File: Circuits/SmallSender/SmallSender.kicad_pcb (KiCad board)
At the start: 2 copper layers, 28 x 57.5 mm, 12 parts, among them CN1 WRITER, SW1 SW_PUSH, SW2 REED SW, U1 LITE_LITE, U2 HN2S01FU

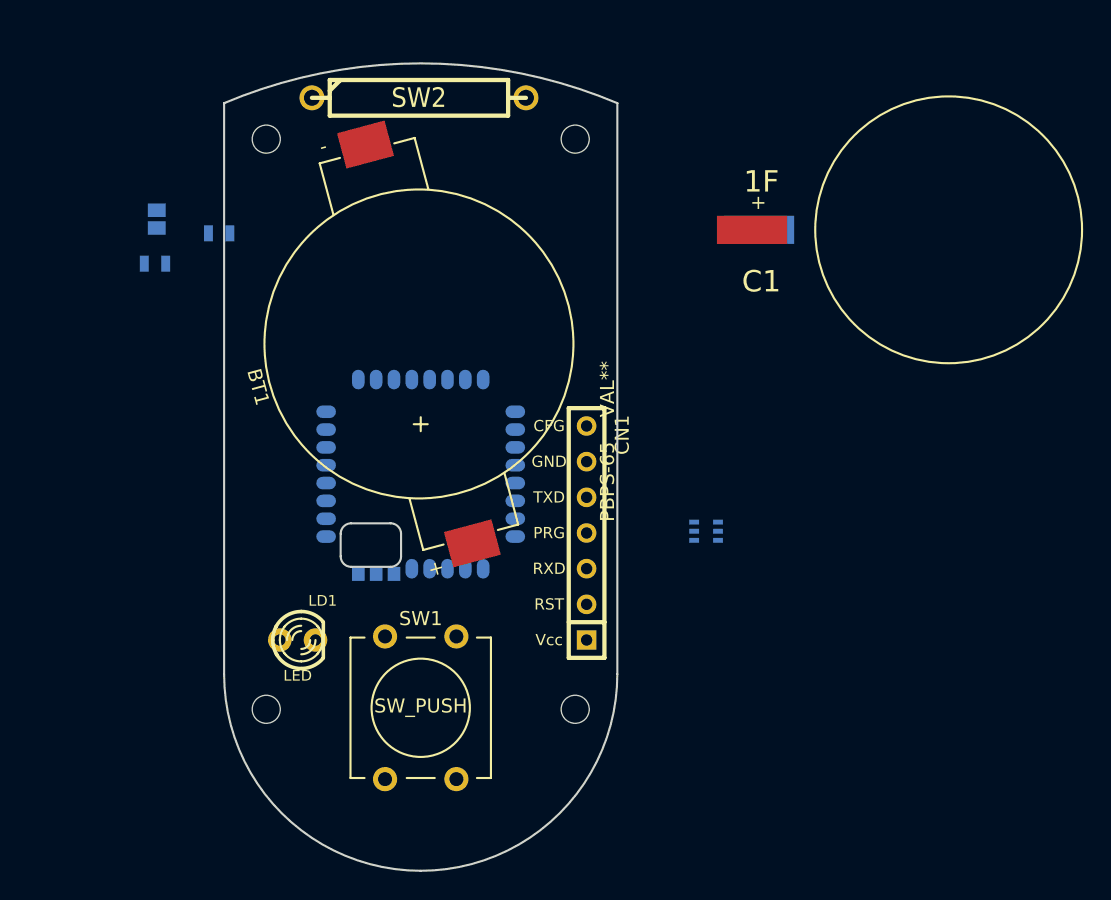
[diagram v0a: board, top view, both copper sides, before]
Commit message: Replaced EDLC.
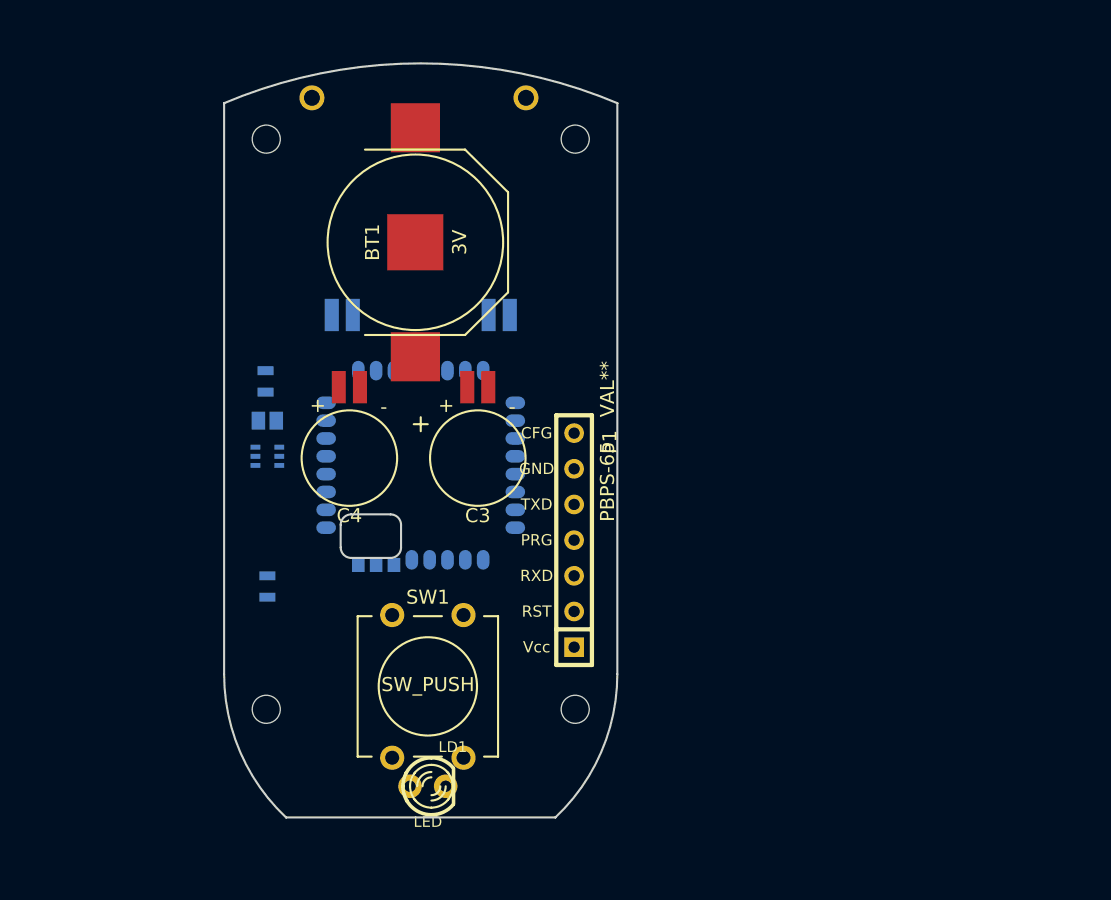
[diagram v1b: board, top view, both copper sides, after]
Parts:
- removed CN1: WRITER, 2211R-07G-LP
- added C2: 0.22, DCK-3R3E224-E, B.Cu at (34.5, 29.0)
- added C3: 0.22, DCK-3R3E224-E, F.Cu at (44.2, 44.2)
- added C4: 0.22, DCK-3R3E224-E, F.Cu at (35.1, 44.2)
- added P1: WRITER-VCC, WRITE-7P, F.Cu at (51.1, 50.0)
- BT1: footprint SMTU2032 -> BK-885
- C1: value 1F -> 0.22; footprint SE-5R5-D105VYV -> DCK-3R3E224-E; moved to B.Cu
- SW2: moved to B.Cu
- U1: value LITE_LITE -> TWE_LITE_SMD
- moved C1 32.0 mm to (45.7, 29.0)
- moved U2 31.7 mm to (29.2, 44.1), turned to 180 degrees
- moved R2 25.4 mm to (29.2, 53.3), turned to 270 degrees
- moved JP1 16.4 mm to (29.2, 41.5), turned to 90 degrees
- moved LD1 13.9 mm to (40.6, 67.6)
- moved R1 11.5 mm to (29.1, 38.7), turned to 270 degrees
- moved BT1 7.24 mm to (39.8, 28.8), turned to 90 degrees
- moved SW1 1.61 mm to (40.6, 60.5)
- moved U1 0.63 mm to (40.1, 44.7)
- turned SW2 to 180 degrees
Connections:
- R2 pad 1: /LED -> /Vcc
- R2 pad 2: /Vcc -> /LED
- U1 pad 12: /M1 -> /CFG
- U1 pad 28: (no net) -> GND
- U1 pad 30: (no net) -> GND
- U1 pad 31: (no net) -> GND
- U1 pad 32: (no net) -> GND
- U1 pad 8: /RX -> /TXD
- U1 pad 9: /TX -> /RXD
- U2 pad 6: /DC3V -> /Vcc
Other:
- board size 28 x 57.5 mm -> 28 x 53.7 mm

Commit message: Added a 3D model of PS-65.
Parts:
- BT1: value 3V -> CR1220

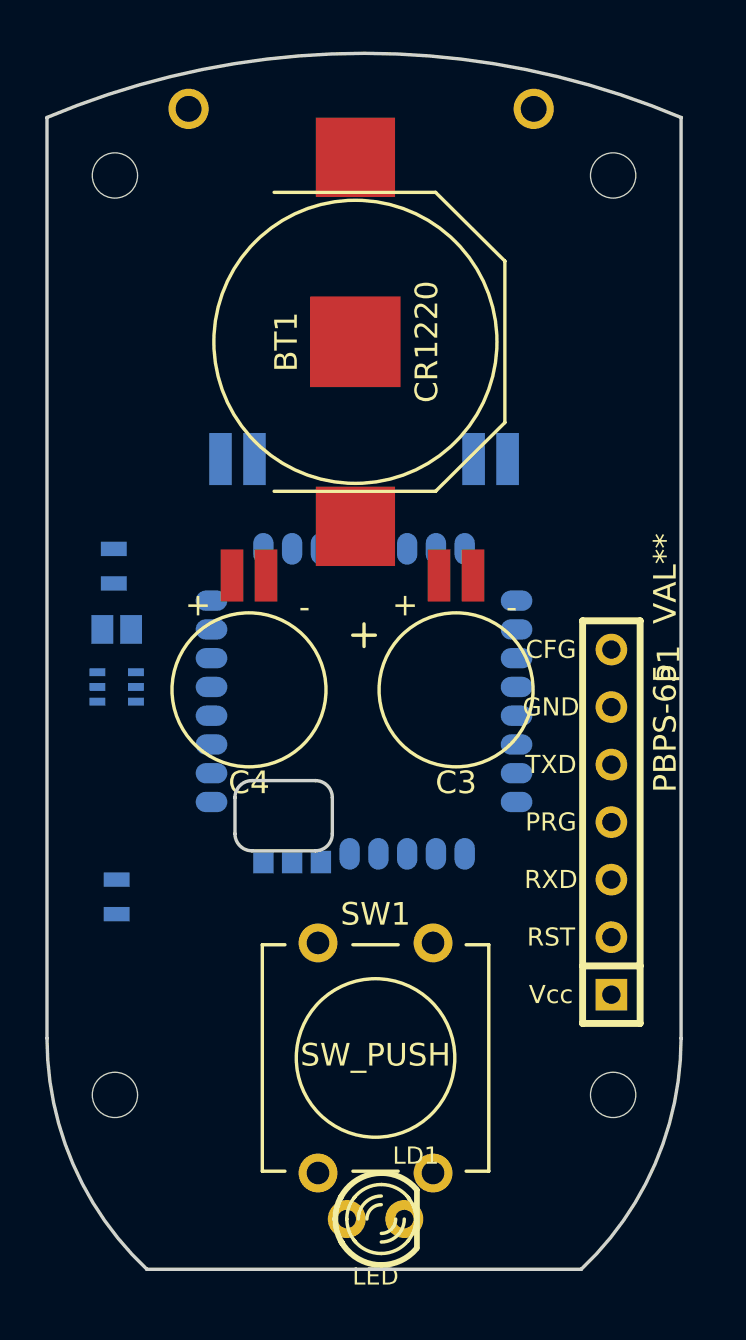
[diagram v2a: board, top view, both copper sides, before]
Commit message: Changed battery holder. Added more EDLC.
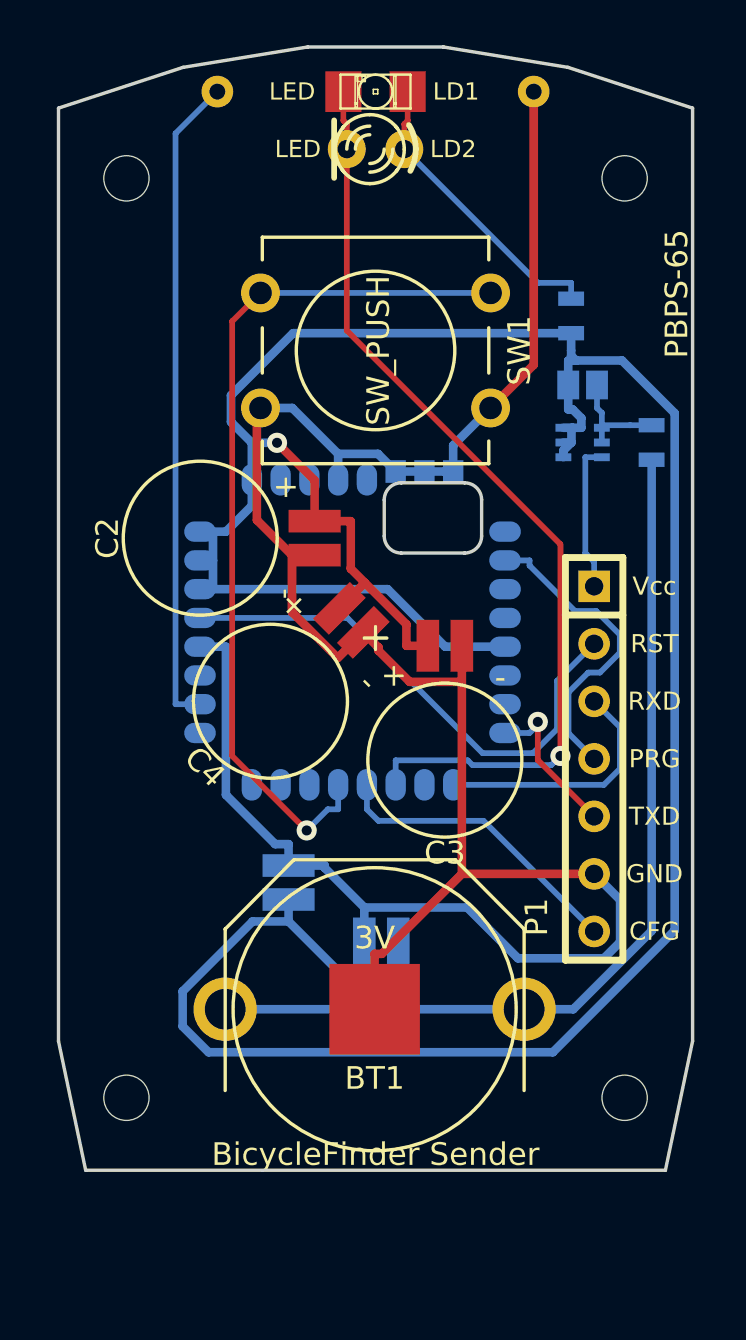
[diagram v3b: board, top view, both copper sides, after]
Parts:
- added C5: 0.22, DCK-3R3E224-E, B.Cu at (31.8, 52.7)
- added LD1: LED, LED-1206, F.Cu at (40.6, 17.8)
- BT1: value CR1220 -> 3V; footprint BK-885 -> BK-890
- C2: moved to F.Cu
- PBPS-65: value VAL** -> BicycleFinder Sender
- SW2: footprint R6 -> REEDSW
- moved LD2 47.2 mm to (40.6, 20.3), turned to 180 degrees
- moved R2 32.6 mm to (49.3, 27.7), turned to 90 degrees
- moved C1 31.9 mm to (40.9, 60.5), turned to 0 degrees
- moved SW1 31.2 mm to (40.6, 29.2), turned to 90 degrees
- moved BT1 29.5 mm to (40.6, 58.3), turned to 180 degrees
- moved R1 24.4 mm to (52.8, 33.3), turned to 90 degrees
- moved JP1 23.2 mm to (49.8, 30.7), turned to 270 degrees
- moved U2 23.2 mm to (49.8, 33.3), turned to 0 degrees
- moved C2 8.70 mm to (32.9, 37.5), turned to 90 degrees
- moved C3 3.14 mm to (43.7, 47.3)
- moved U1 3.09 mm to (39.6, 41.7), turned to 180 degrees
- moved P1 2.90 mm to (50.3, 47.2), turned to 270 degrees
- moved C4 1.07 mm to (36.0, 44.7), turned to 135 degrees
- moved SW2 0.99 mm to (40.6, 17.8), turned to 0 degrees
- moved PBPS-65 0.52 mm to (40.6, 41.9)
- renumbered LD1 to LD2
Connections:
- C4 pad 1: (no net) -> /Vcc
- P1 pad 1: /Vcc -> /3V3
- U1 pad 22: (no net) -> /Vcc
- U1 pad 23: (no net) -> /Vcc
- U1 pad 24: (no net) -> /Vcc
- U1 pad 25: (no net) -> /Vcc
- U2 pad 6: /Vcc -> /3V3
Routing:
- net /Vcc: track 0.00 -> 133.9 mm, vias 0 -> 1
- net GND: track 0.00 -> 107.3 mm
- net /DO4: track 0.00 -> 41.9 mm, vias 0 -> 1
- net /3V: track 0.00 -> 41.1 mm
- net /DI1: track 0.00 -> 38.6 mm, vias 0 -> 1
- net /DI4: track 0.00 -> 28.9 mm
- net /RST: track 0.00 -> 23.1 mm
- net /PRG: track 0.00 -> 13.8 mm
- net /CFG: track 0.00 -> 13.3 mm
- net /LED: track 0.00 -> 13.1 mm
- net /RXD: track 0.00 -> 11.1 mm
- net /TXD: track 0.00 -> 6.92 mm, vias 0 -> 1
- net /3V3: track 0.00 -> 6.59 mm
- net /CHG: track 0.00 -> 4.83 mm
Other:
- board size 28 x 53.7 mm -> 28 x 49.6 mm
- net class Power added: clearance 0.254, trace_width 0.381, via_dia 0.889, via_drill 0.635

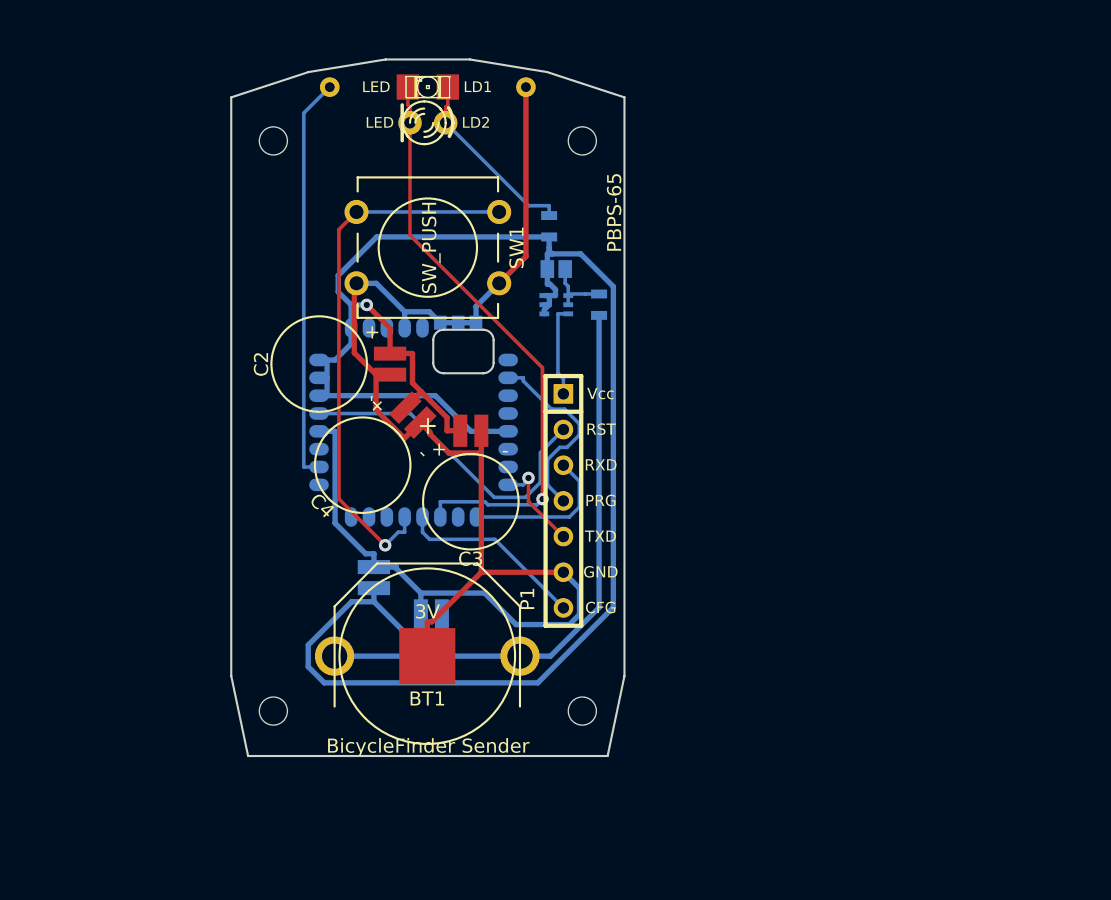
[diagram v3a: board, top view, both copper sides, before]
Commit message: Changed EDLC.
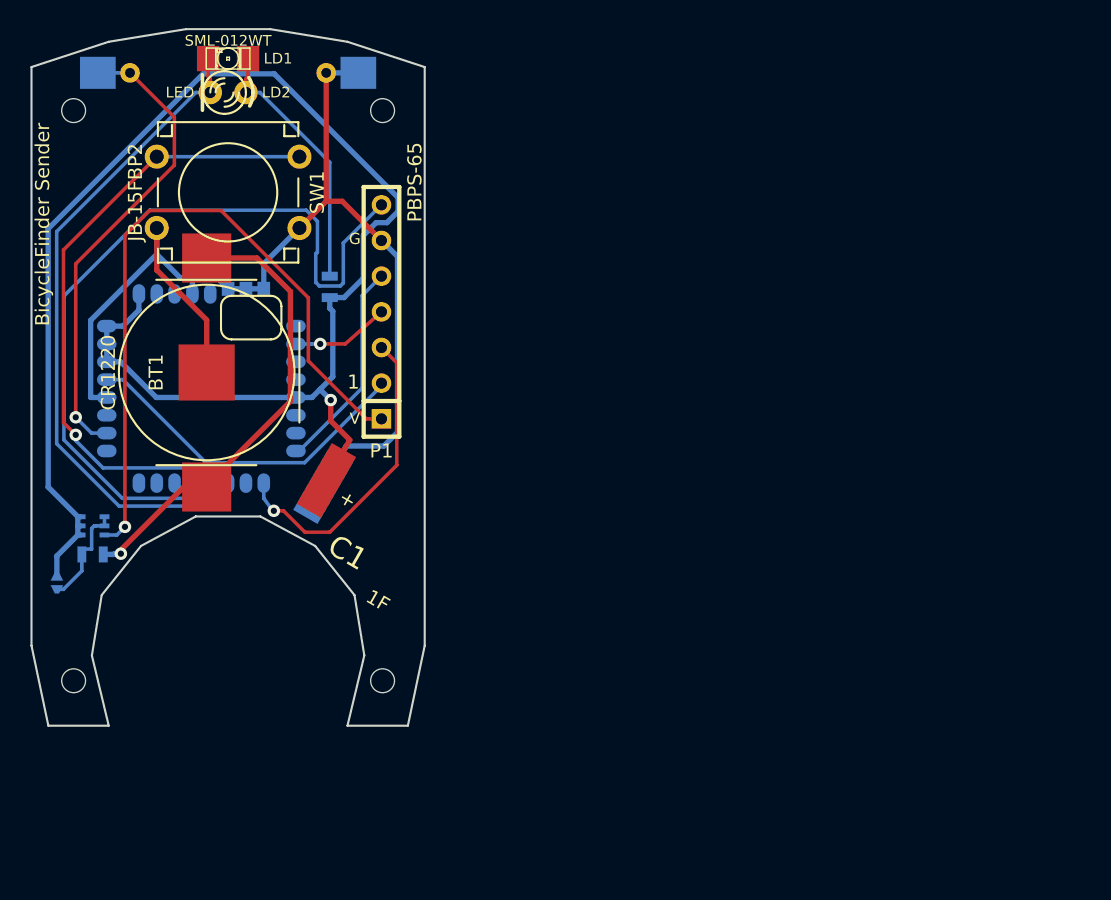
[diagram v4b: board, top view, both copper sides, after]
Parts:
- removed C2, C3, C4, C5: 0.22, DCK-3R3E224-E
- BT1: value 3V -> CR1220; footprint BK-890 -> BK-885
- C1: value 0.22 -> 1F; footprint DCK-3R3E224-E -> SE-5R5-D105VYV; moved to F.Cu
- JP1: footprint GS2 -> JUMPER
- LD1: value LED -> SML-012WT
- PBPS-65: footprint PBPS-65 -> PBPS-65+EDLC
- SW1: value SW_PUSH -> JB-15FBP2
- SW2: value REED SW -> MKA-10110
- U1: footprint TWE-001L-NC7 -> TWE-001L-SMD-noNTH
- moved JP1 42.0 mm to (14.2, 53.1)
- moved R1 40.2 mm to (16.8, 51.1), turned to 180 degrees
- moved U2 36.6 mm to (16.8, 49.0)
- moved BT1 25.6 mm to (24.9, 38.1), turned to 90 degrees
- moved P1 18.7 mm to (37.3, 33.8), turned to 90 degrees
- moved R2 16.2 mm to (33.7, 32.0)
- moved U1 15.3 mm to (24.5, 39.2)
- moved SW1 14.8 mm to (26.4, 25.3)
- moved C1 14.7 mm to (26.4, 57.9), turned to 60 degrees
- moved LD2 14.4 mm to (26.4, 18.2)
- moved PBPS-65 14.4 mm to (26.4, 39.8)
- moved LD1 14.4 mm to (26.4, 15.7)
- moved SW2 14.3 mm to (26.4, 16.8)
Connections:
- P1 pad 1: /3V3 -> /RST
- P1 pad 2: /RST -> /RXD
- P1 pad 3: /RXD -> /PRG
- P1 pad 4: /PRG -> /TXD
- P1 pad 5: /TXD -> GND
- P1 pad 6: GND -> /CFG
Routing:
- net /CFG: track 13.3 -> 57.6 mm
- net /3V3: track 6.59 -> 50.2 mm, vias 0 -> 1
- net /Vcc: track 133.9 -> 107.9 mm
- net GND: track 107.3 -> 82.8 mm
- net /RXD: track 11.1 -> 22.1 mm, vias 0 -> 1
- net /3V: track 41.1 -> 32.9 mm, vias 0 -> 1
- net /TXD: track 6.92 -> 15.1 mm, vias 1 -> 0
- net /PRG: track 13.8 -> 6.96 mm, vias 0 -> 1
- net /DO4: track 41.9 -> 48.0 mm, vias 1 -> 0
- net /LED: track 13.1 -> 18.6 mm
- net /DI1: track 38.6 -> 43.7 mm
- net /DI4: track 28.9 -> 33.7 mm, vias 0 -> 1
- net /CHG: track 4.83 -> 7.68 mm
- net /RST: track 23.1 -> 24.5 mm
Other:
- outline, holes or cut-outs redrawn

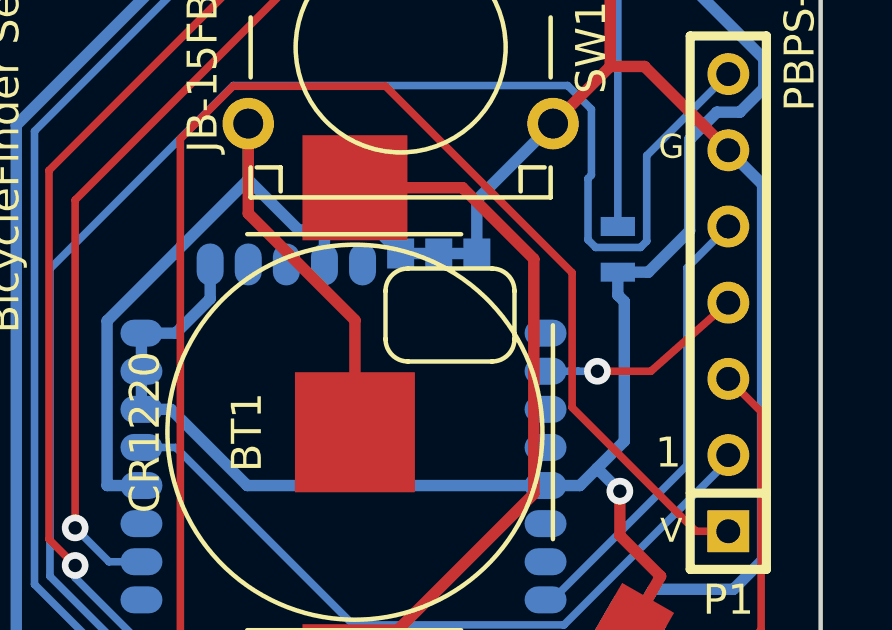
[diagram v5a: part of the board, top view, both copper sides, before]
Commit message: Fixed: Model with NPH hole.
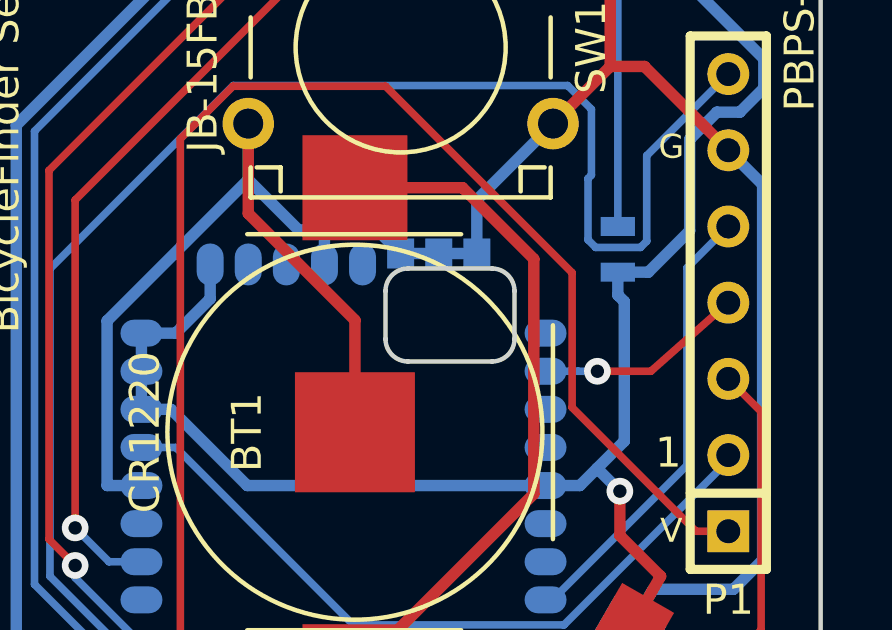
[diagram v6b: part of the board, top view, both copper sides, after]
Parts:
- U1: footprint TWE-001L-SMD-noNTH -> TWE-001L-NC7
